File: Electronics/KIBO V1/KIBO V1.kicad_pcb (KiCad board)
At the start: 2 copper layers, 28 parts, among them M17 Fan, Q1 TIP120, Q2 TIP120, Q3 TIP120, Q4 TIP120, SW1 SW_SPST, U1 HC-SR04, U10 UBEC, U11 uSwitch, U13 uSwitch, U14 uSwitch, U15 uSwitch, U16 PWMDriver, U2 PortExt, U3 ESP32-DEVKITC, U4 GY-521, U5 DM-OLED096-636, U7 VoltConv, U8 MotorDriver, U9 MotorDriver

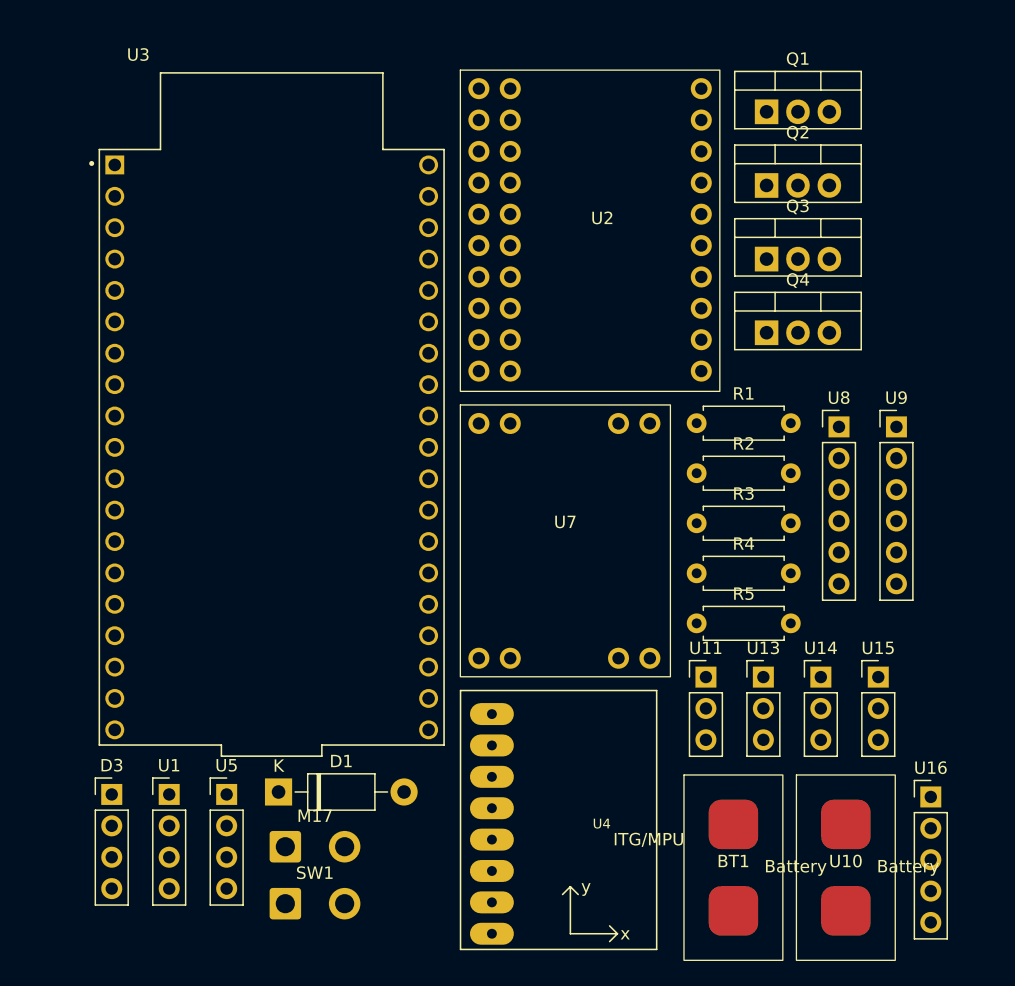
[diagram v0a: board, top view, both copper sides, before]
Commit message: feat: added push buttons, batt measu and hc-sr04 esp32cam to schematic and footprints
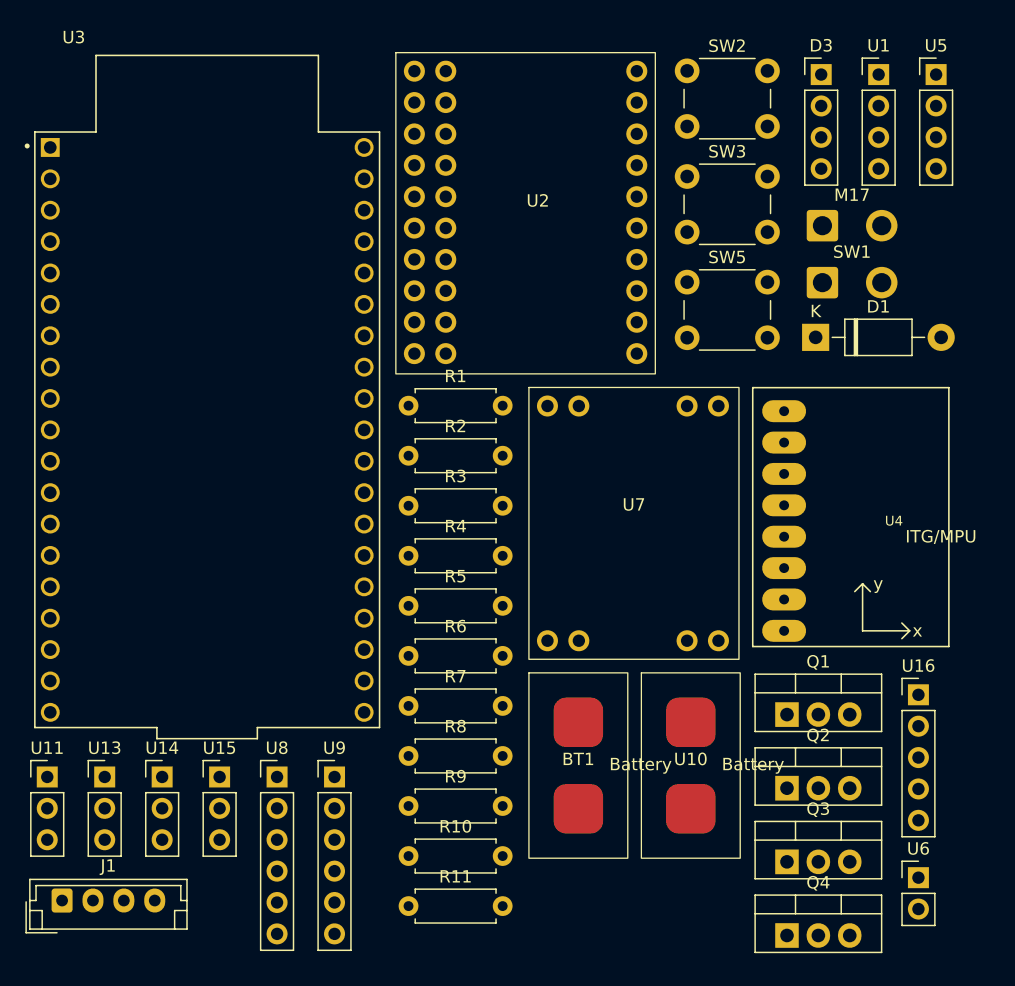
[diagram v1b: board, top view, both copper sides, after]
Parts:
- added J1: Conn_01x04, Connector_JST:JST_EH_B4B-EH-A_1x04_P2.50mm_Vertical, F.Cu at (101.2, 111.3)
- added R10: 5k6, Resistor_THT:R_Axial_DIN0207_L6.3mm_D2.5mm_P7.62mm_Horizontal, F.Cu at (129.2, 107.7)
- added R11: 2k, Resistor_THT:R_Axial_DIN0207_L6.3mm_D2.5mm_P7.62mm_Horizontal, F.Cu at (129.2, 111.8)
- added R6: 5k6, Resistor_THT:R_Axial_DIN0207_L6.3mm_D2.5mm_P7.62mm_Horizontal, F.Cu at (129.2, 91.5)
- added R7: 22k, Resistor_THT:R_Axial_DIN0207_L6.3mm_D2.5mm_P7.62mm_Horizontal, F.Cu at (129.2, 95.6)
- added R8: 1k, Resistor_THT:R_Axial_DIN0207_L6.3mm_D2.5mm_P7.62mm_Horizontal, F.Cu at (129.2, 99.6)
- added R9: 680, Resistor_THT:R_Axial_DIN0207_L6.3mm_D2.5mm_P7.62mm_Horizontal, F.Cu at (129.2, 103.7)
- added SW2: SW_Push, Button_Switch_THT:SW_PUSH_6mm, F.Cu at (151.8, 44.2)
- added SW3: SW_Push, Button_Switch_THT:SW_PUSH_6mm, F.Cu at (151.8, 52.7)
- added SW5: SW_Push, Button_Switch_THT:SW_PUSH_6mm, F.Cu at (151.8, 61.3)
- added U6: ESP32-CAM, Connector_PinHeader_2.54mm:PinHeader_1x02_P2.54mm_Vertical, F.Cu at (170.5, 109.5)
- moved D3 81.8 mm to (162.6, 44.5)
- moved U1 81.8 mm to (167.3, 44.5)
- moved U5 81.8 mm to (171.9, 44.5)
- moved M17 66.5 mm to (162.7, 56.7)
- moved SW1 66.5 mm to (162.7, 61.3)
- moved D1 57.0 mm to (162.2, 65.7)
- moved U11 53.9 mm to (100.0, 101.3)
- moved U15 53.9 mm to (113.9, 101.3)
- moved U13 53.9 mm to (104.6, 101.3)
- moved U14 53.9 mm to (109.3, 101.3)
- moved U9 53.6 mm to (123.2, 101.3)
- moved U8 53.6 mm to (118.6, 101.3)
- moved Q1 48.8 mm to (159.9, 96.3)
- moved Q3 48.8 mm to (159.9, 108.2)
- moved Q2 48.8 mm to (159.9, 102.2)
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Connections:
- U3 pad 12: unconnected-(U3-IO14-Pad12) -> /SW2
- U3 pad 23: unconnected-(U3-IO15-Pad23) -> /SW1
- U3 pad 5: unconnected-(U3-IO34-Pad5) -> /CLL1
- U3 pad 6: unconnected-(U3-IO35-Pad6) -> /CLL2
- U3 pad 7: unconnected-(U3-IO32-Pad7) -> /CLL3
- U3 pad 8: unconnected-(U3-IO33-Pad8) -> /SW3

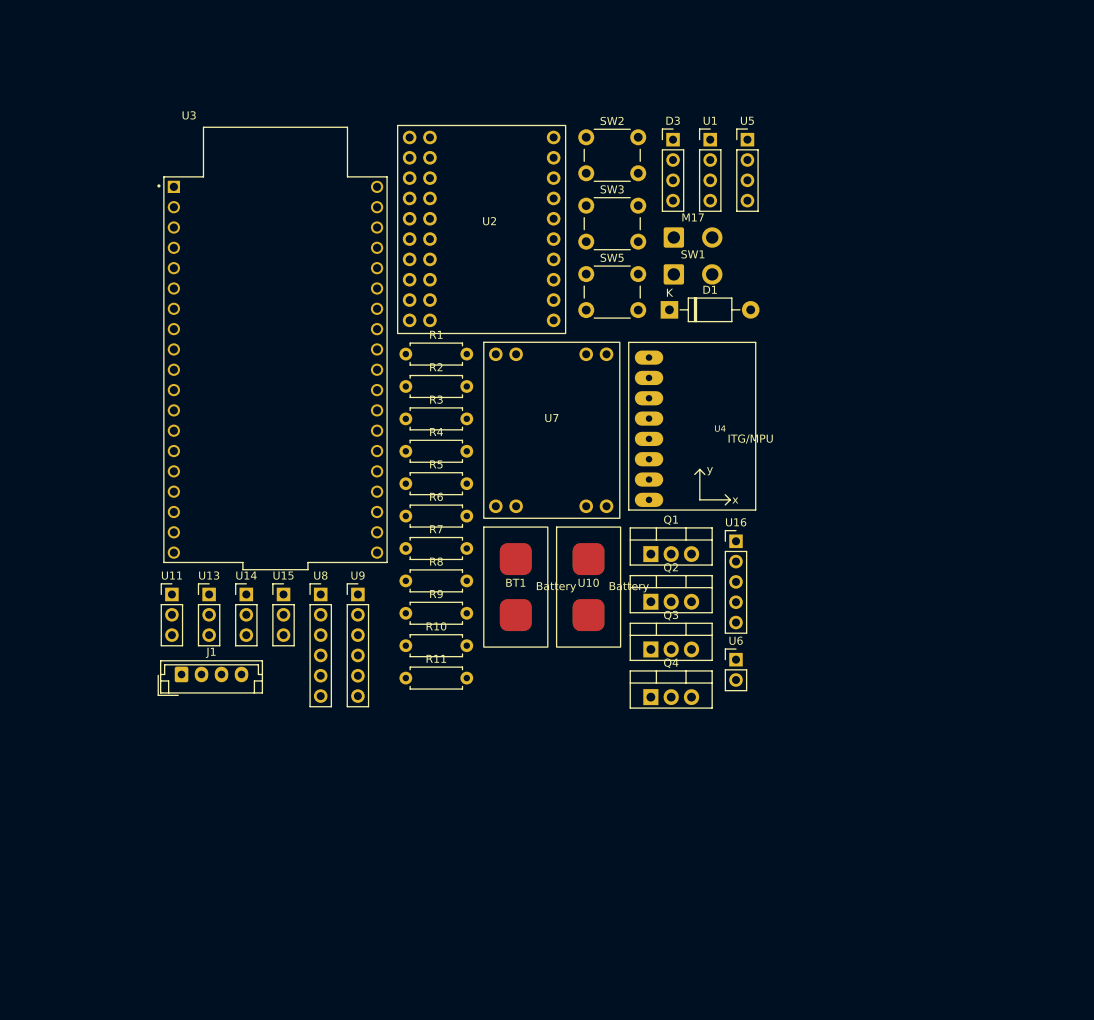
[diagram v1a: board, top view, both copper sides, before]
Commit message: feat: setup PCB size, holes and all U components
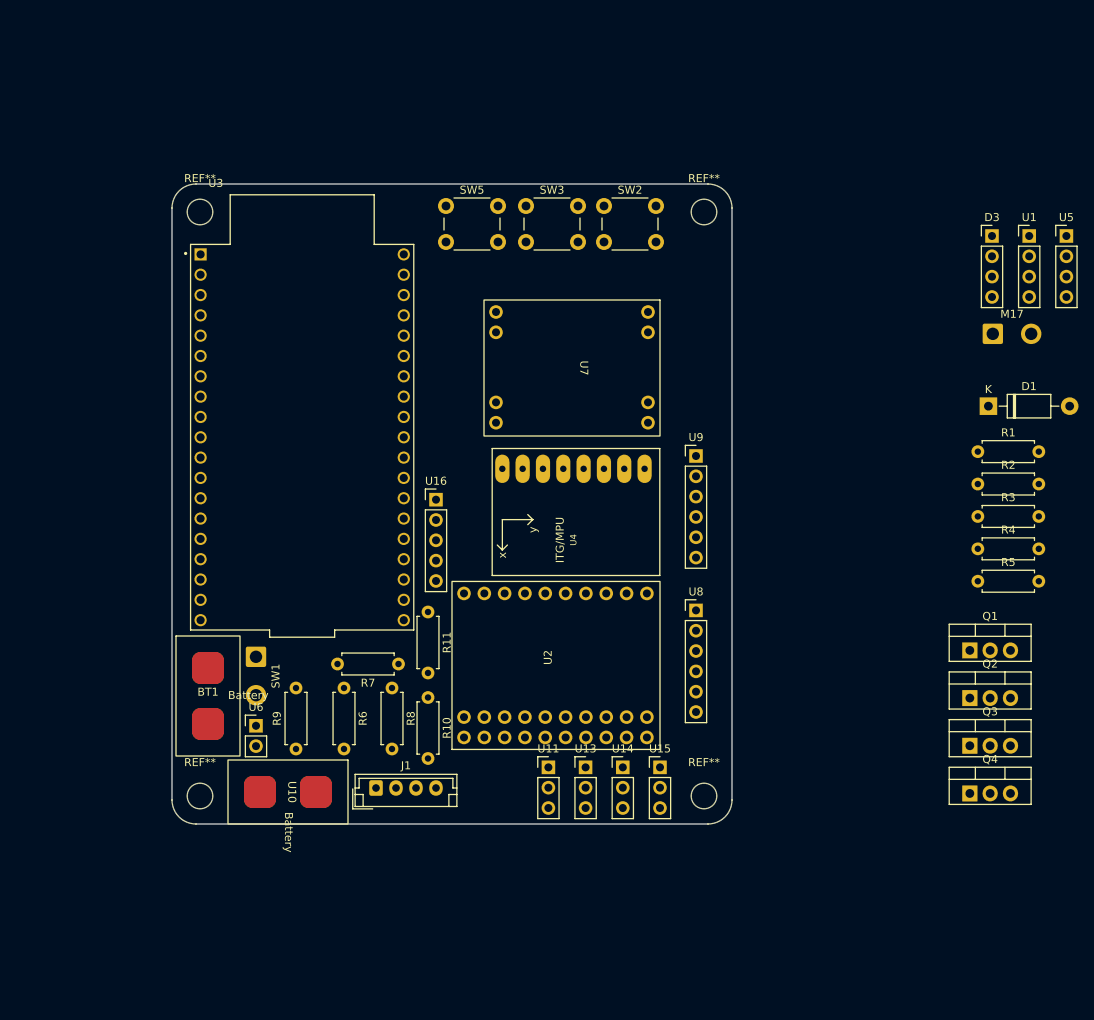
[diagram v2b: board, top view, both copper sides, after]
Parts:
- added REF**: MountingHole_3.2mm_M3, MountingHole:MountingHole_3.2mm_M3, F.Cu at (166.5, 126.5)
- added REF**: MountingHole_3.2mm_M3, MountingHole:MountingHole_3.2mm_M3, F.Cu at (166.5, 53.5)
- added REF**: MountingHole_3.2mm_M3, MountingHole:MountingHole_3.2mm_M3, F.Cu at (103.5, 126.5)
- added REF**: MountingHole_3.2mm_M3, MountingHole:MountingHole_3.2mm_M3, F.Cu at (103.5, 53.5)
- moved U2 75.3 mm to (136.5, 119.2), turned to 90 degrees
- moved R1 72.5 mm to (200.7, 83.5)
- moved R2 72.5 mm to (200.7, 87.5)
- moved R3 72.5 mm to (200.7, 91.6)
- moved R4 72.5 mm to (200.7, 95.6)
- moved R5 72.5 mm to (200.7, 99.7)
- moved SW1 70.8 mm to (110.5, 109.1), turned to -90 degrees
- moved U6 60.6 mm to (110.5, 117.7)
- moved U11 51.8 mm to (147.1, 122.9)
- moved U15 51.8 mm to (161.0, 122.9)
- moved U13 51.8 mm to (151.7, 122.9)
- moved U14 51.8 mm to (156.3, 122.9)
- moved U8 47.0 mm to (165.5, 103.3)
- moved U9 45.7 mm to (165.5, 84.0)
- moved U10 45.5 mm to (114.5, 126.0), turned to -90 degrees
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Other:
- board outline added: 70 x 80 mm

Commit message: feat: final position of all footprints on PCB
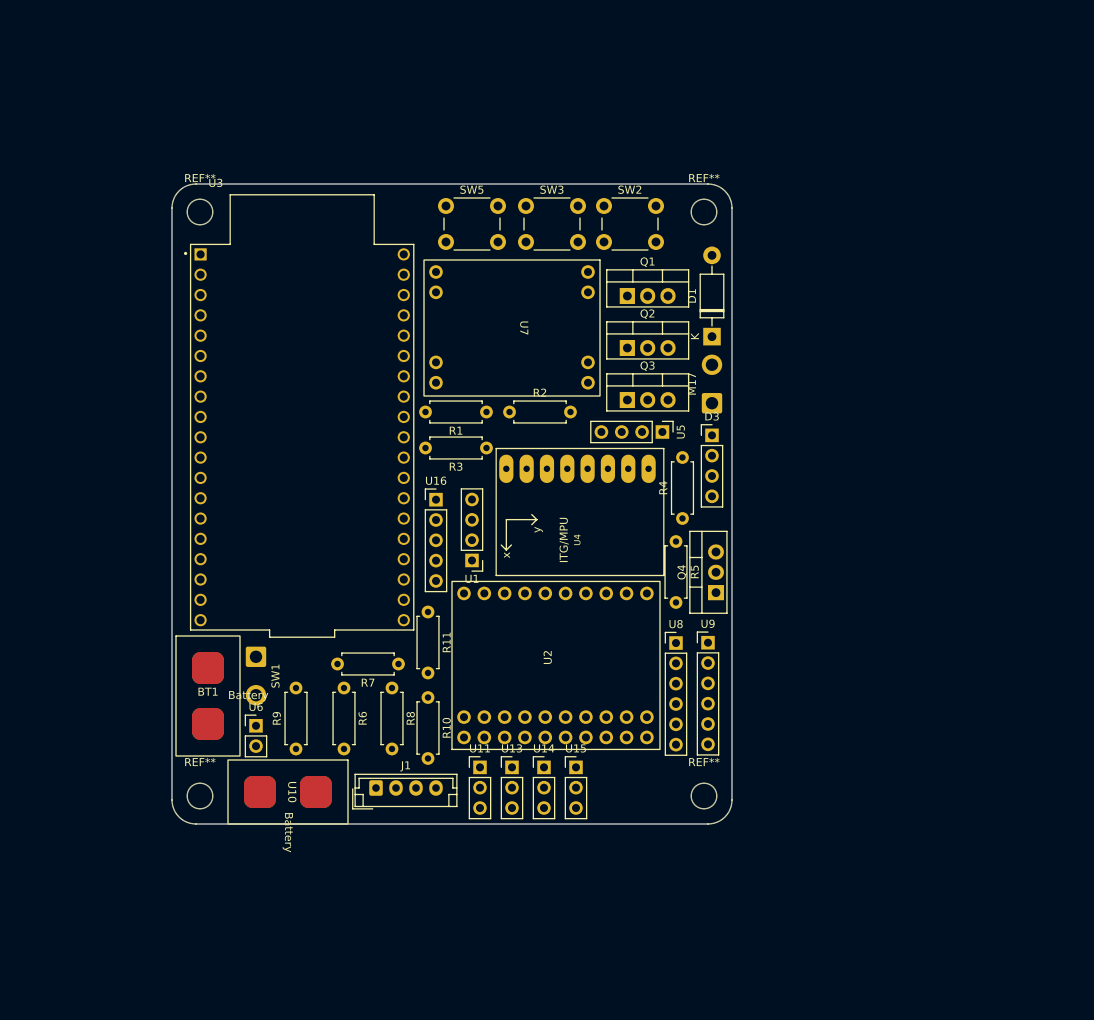
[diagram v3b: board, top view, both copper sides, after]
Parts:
- moved U1 80.6 mm to (137.5, 97.1), turned to 180 degrees
- moved R3 62.0 mm to (139.3, 83.0), turned to 180 degrees
- moved R1 61.6 mm to (139.3, 78.5), turned to 180 degrees
- moved Q1 61.6 mm to (156.9, 64.0)
- moved Q2 61.2 mm to (156.9, 70.5)
- moved Q3 60.8 mm to (156.9, 77.0)
- moved R2 59.2 mm to (142.2, 78.5)
- moved U5 56.1 mm to (161.3, 81.0), turned to -90 degrees
- moved D3 43.0 mm to (167.5, 81.4)
- moved Q4 40.5 mm to (168.0, 101.1), turned to 90 degrees
- moved R5 38.1 mm to (163.0, 94.7), turned to -90 degrees
- moved R4 37.1 mm to (163.8, 91.8), turned to 90 degrees
- moved M17 36.2 mm to (167.5, 77.4), turned to 90 degrees
- moved D1 35.6 mm to (167.5, 69.1), turned to 90 degrees
- moved U9 23.4 mm to (167.0, 107.3)
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
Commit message: fix: cleaned footprint placement, text and logos
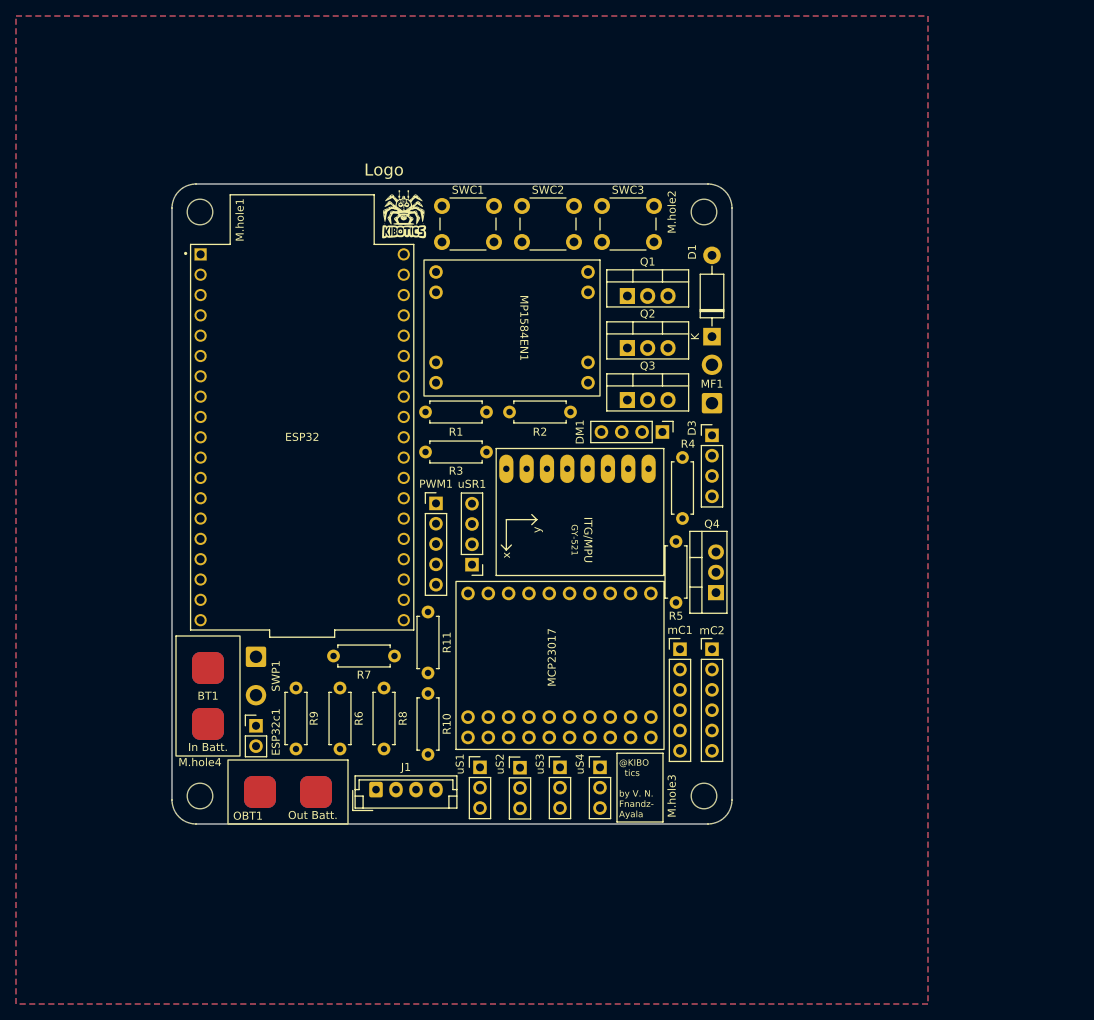
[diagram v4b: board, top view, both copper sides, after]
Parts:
- added Logo: LOGO, LOGO, F.Cu at (129.0, 53.8)
- DM1: renamed from U5; value DM-OLED096-636 -> DM-OLED
- PWM1: renamed from U16; value PWMDriver -> PWM
- SWP1: renamed from SW1; value SW_SPST -> SWP
- moved SWC2 10.2 mm to (143.8, 52.8)
- moved SWC3 9.50 mm to (153.8, 52.8)
- moved uS4 3.00 mm to (153.5, 122.9)
- moved uS3 2.00 mm to (148.5, 122.9)
- moved R7 1.12 mm to (127.8, 109.0)
- moved uS2 1.00 mm to (143.5, 123.0)
- moved R8 1.00 mm to (126.5, 113.0)
- moved mC2 0.95 mm to (167.5, 108.2)
- moved mC1 0.92 mm to (163.5, 108.2)
- moved uSR1 0.52 mm to (137.5, 97.6)
- moved MCP23017 0.50 mm to (137.0, 119.2)
- moved R10 0.50 mm to (132.0, 113.7)
- moved R3 0.50 mm to (139.3, 83.5)
- moved R6 0.50 mm to (121.0, 113.0)
- moved SWC1 0.50 mm to (133.8, 52.8)
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- renumbered U3 to ESP32, U6 to ESP32c1, U4 to GY-521, REF** to M.hole1, REF** to M.hole2, REF** to M.hole3, REF** to M.hole4, U2 to MCP23017, M17 to MF1, U7 to MP1584EN1, U10 to OBT1, SW5 to SWC1, SW2 to SWC2, SW3 to SWC3, U8 to mC1, U9 to mC2, U11 to uS1, U13 to uS2, U14 to uS3, U15 to uS4, U1 to uSR1
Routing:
- added copper zone on B.Cu, net GND
- added copper zone on F.Cu, net GND
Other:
- board text added: "@KIBO tics by V. N. Fnandz- Ayala"

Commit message: feat: finished PCB and its CAD
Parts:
- moved OBT1 0.10 mm to (114.5, 125.9)
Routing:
- net +11V1: track 0.00 -> 173.6 mm
- net +3V3: track 0.00 -> 161.6 mm, vias 0 -> 1
- net /FAN: track 0.00 -> 147.8 mm, vias 0 -> 2
- net /M3EN: track 0.00 -> 101.5 mm
- net /M4EN: track 0.00 -> 99.5 mm, vias 0 -> 1
- net /SCL: track 0.00 -> 92.2 mm, vias 0 -> 1
- net +5V: track 0.00 -> 91.9 mm, vias 0 -> 2
- net /M2EN: track 0.00 -> 87.4 mm
- net /SDA: track 0.00 -> 86.0 mm
- net /SW3: track 0.00 -> 67.8 mm
- net /M1EN: track 0.00 -> 62.6 mm, vias 0 -> 2
- net /SW2: track 0.00 -> 61.6 mm
- net /CLL3: track 0.00 -> 61.4 mm
- net /CLL2: track 0.00 -> 59.6 mm
- net /SW1: track 0.00 -> 54.3 mm
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
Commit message: fix: added polarity sign to battery pads
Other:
- board text added: "+"
- board text added: "-"
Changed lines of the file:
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@@
 		(layer "Edge.Cuts")
+	)
+	(gr_text "+"
+		(at 100.75 111 0)
+		(layer "F.SilkS")
+		(effects
+			(font
+				(size 1 1)
+				(thickness 0.1)
+			)
+			(justify left bottom)
+		)
 	)
 	(gr_text "@KIBO\n  tics\n\nby V. N. \nFnandz-\nAyala"
@@
 			)
 			(justify left bottom)
+		)
+	)
+	(gr_text "-"
+		(at 107.25 126.5 0)
+		(layer "F.SilkS")
+		(effects
+			(font
+				(size 1 1)
+				(thickness 0.1)
+			)
+			(justify left bottom)
+		)
+	)
+	(gr_text "-"
+		(at 134.7 64.05 0)
+		(layer "F.SilkS")
+		(effects
+			(font
+				(size 1 1)
+				(thickness 0.1)
+			)
+			(justify left bottom)
+		)
+	)
+	(gr_text "-"
+		(at 100.75 118 0)
+		(layer "F.SilkS")
+		(effects
+			(font
+				(size 1 1)
+				(thickness 0.1)
+			)
+			(justify left bottom)
+		)
+	)
+	(gr_text "+"
+		(at 149 72.8 0)
+		(layer "F.SilkS")
+		(effects
+			(font
+				(size 1 1)
+				(thickness 0.1)
+			)
+			(justify left bottom)
+		)
+	)
+	(gr_text "-"
+		(at 149 64.05 0)
+		(layer "F.SilkS")
+		(effects
+			(font
+				(size 1 1)
+				(thickness 0.1)
+			)
+			(justify left bottom)
+		)
+	)
+	(gr_text "-"
+		(at 149 61.5 0)
+		(layer "F.SilkS")
+		(effects
+			(font
+				(size 1 1)
+				(thickness 0.1)
+			)
+			(justify left bottom)
+		)
+	)
+	(gr_text "+"
+		(at 149 75.35 0)
+		(layer "F.SilkS")
+		(effects
+			(font
+				(size 1 1)
+				(thickness 0.1)
+			)
+			(justify left bottom)
+		)
+	)
+	(gr_text "-"
+		(at 134.7 61.5 0)
+		(layer "F.SilkS")
+		(effects
+			(font
+				(size 1 1)
+				(thickness 0.1)
+			)
+			(justify left bottom)
+		)
+	)
+	(gr_text "+"
+		(at 120.5 126.5 0)
+		(layer "F.SilkS")
+		(effects
+			(font
+				(size 1 1)
+				(thickness 0.1)
+			)
+			(justify left bottom)
+		)
+	)
+	(gr_text "+"
+		(at 134.7 75.35 0)
+		(layer "F.SilkS")
+		(effects
+			(font
+				(size 1 1)
+				(thickness 0.1)
+			)
+			(justify left bottom)
+		)
+	)
+	(gr_text "+"
+		(at 134.7 72.8 0)
+		(layer "F.SilkS")
+		(effects
+			(font
+				(size 1 1)
+				(thickness 0.1)
+			)
+			(justify left bottom)
